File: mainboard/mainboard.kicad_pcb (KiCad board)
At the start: 2 copper layers, 393.7 x 228.6 mm, 126 parts, among them J1 Conn_01x06, J2 Conn_01x04, J3 EDAC 305-044-520-201

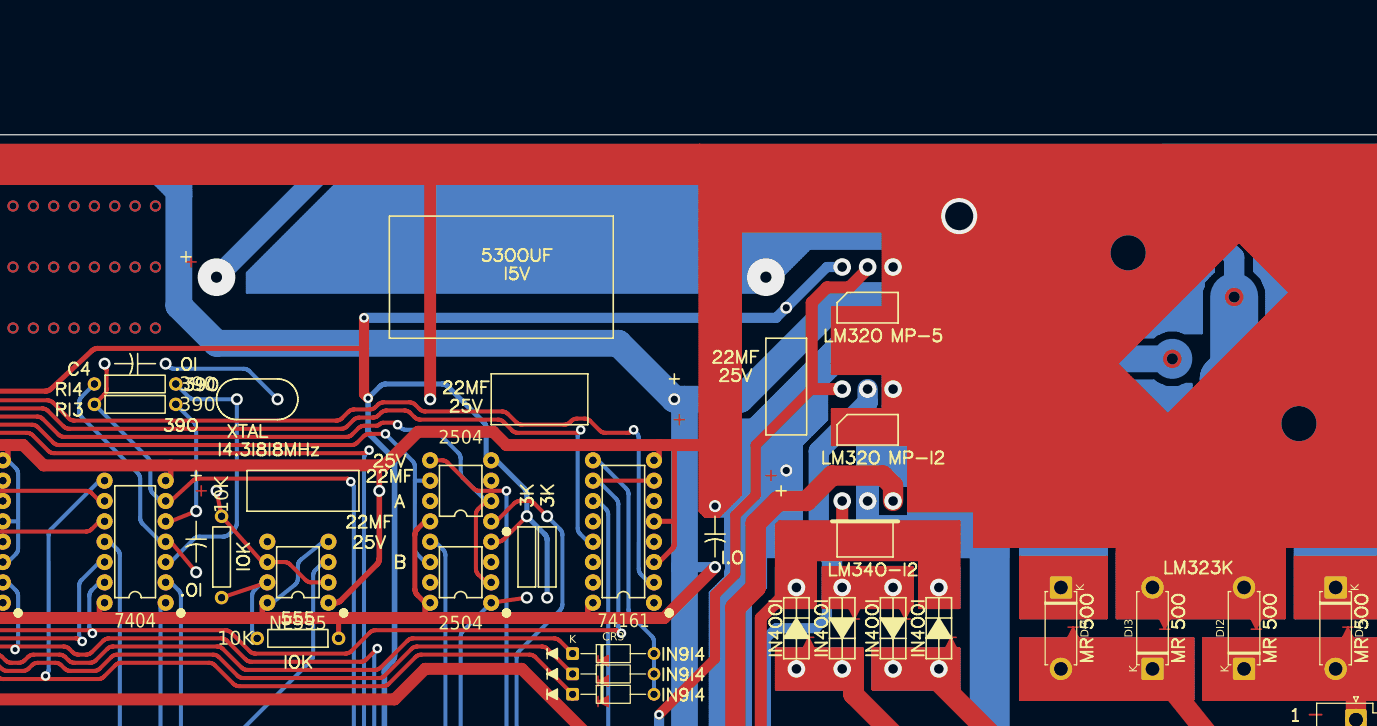
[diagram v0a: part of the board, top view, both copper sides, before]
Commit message: large renaming, tidying up files, old libraries
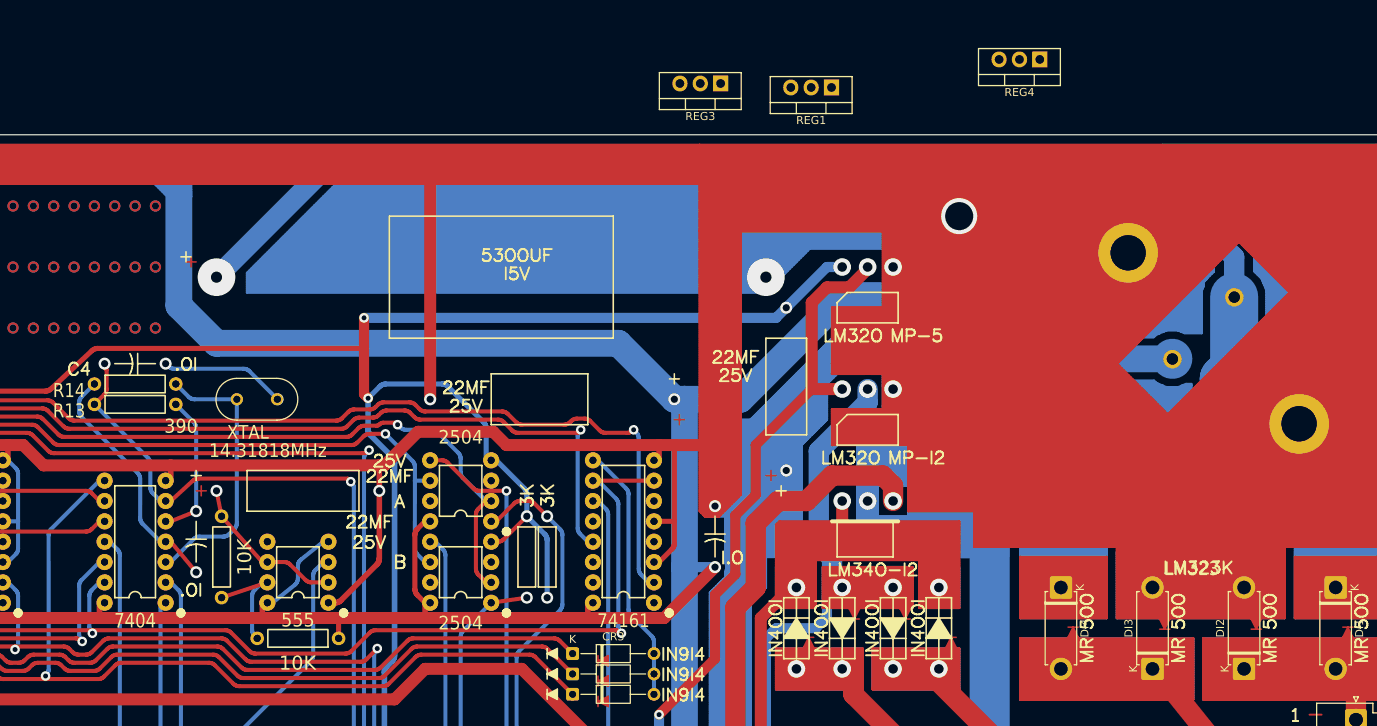
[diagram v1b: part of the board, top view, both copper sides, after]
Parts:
- added REG1: LM320 MP-5, Package_TO_SOT_THT:TO-220-3_Vertical, F.Cu at (324.4, -234.5)
- added REG2: LM323, mainboard:TO-3, F.Cu at (374.7, -208.3)
- added REG3: LM320 MP-12, Package_TO_SOT_THT:TO-220-3_Vertical, F.Cu at (310.6, -235.0)
- added REG4: LM340 MP-12, Package_TO_SOT_THT:TO-220-3_Vertical, F.Cu at (350.4, -238.0)
- added XTAL: 14.31818 MHz, Crystal:Resonator-2Pin_W10.0mm_H5.0mm, F.Cu at (250.2, -195.6)
- D13: value NE555 -> 555
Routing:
- net Net-(CAP4-~-Pad1): track 0.00 -> 15.7 mm, vias 0 -> 2
- net (no net): track 3361.6 -> 3345.9 mm, vias 201 -> 199
